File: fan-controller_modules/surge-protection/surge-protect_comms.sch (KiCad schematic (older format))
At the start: 17 parts

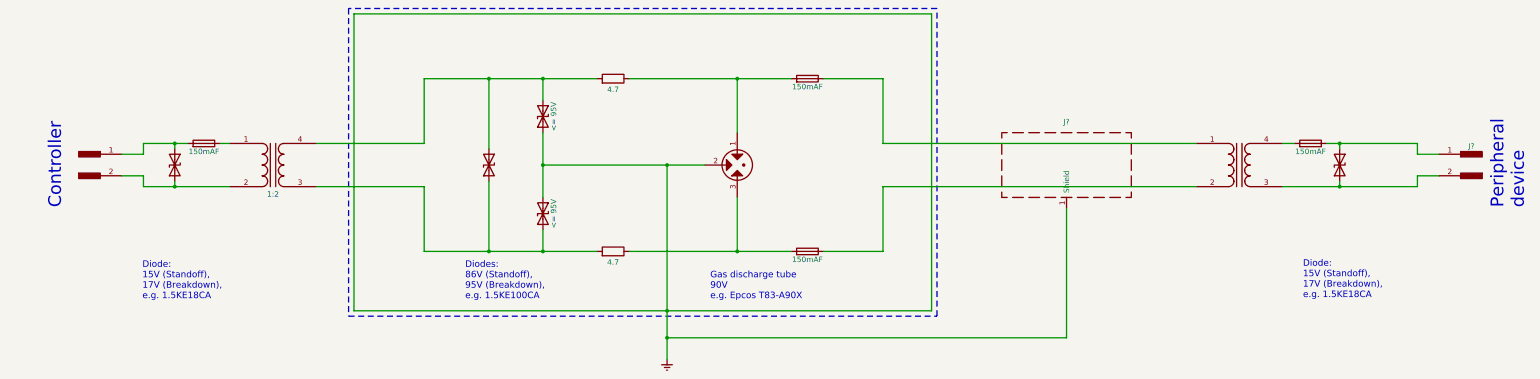
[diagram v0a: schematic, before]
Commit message: Modifying surge protection.
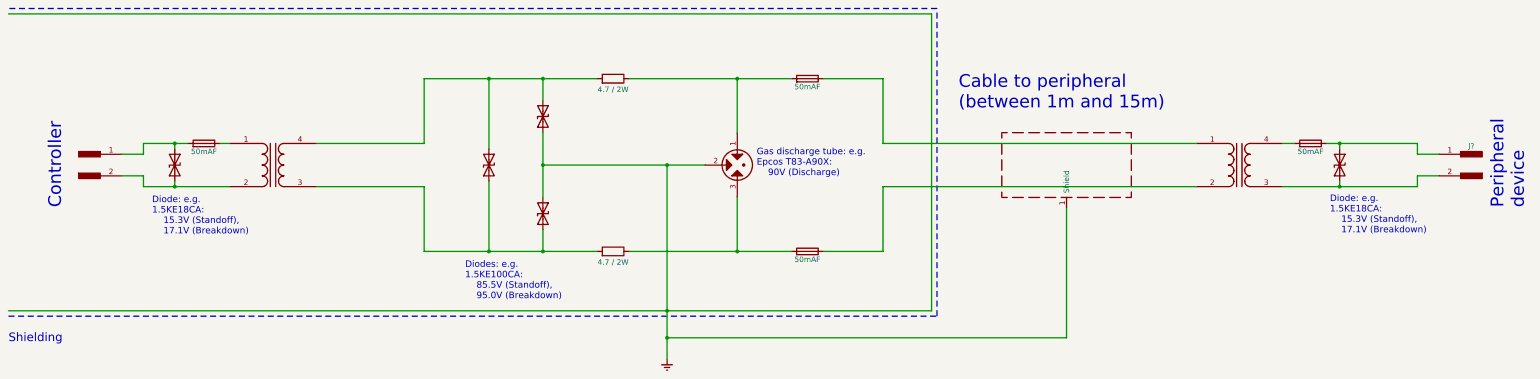
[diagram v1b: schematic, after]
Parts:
- F? (x4): value 150mAF -> 50mAF
- R? (x2): value 4.7 -> 4.7 / 2W
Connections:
- wire segments 47 -> 61
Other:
- note added: "Cable to peripheral\n(between 1m and 15m)"
- note added: "Diode: e.g. \n1.5KE18CA:\n 15.3V (Standoff),\n 17.1V (Breakdown)"
- note added: "Diode: e.g.\n1.5KE18CA:\n 15.3V (Standoff),\n 17.1V (Breakdown)"
- note added: "Diodes: e.g. \n1.5KE100CA:\n 85.5V (Standoff),\n 95.0V (Breakdown)"
- note added: "Gas discharge tube: e.g.\nEpcos T83-A90X:\n 90V (Discharge)"
- note added: "Shielding"
- note removed: "Diode: \n15V (Standoff),\n17V (Breakdown),\ne.g. 1.5KE18CA"
- note removed: "Diodes: \n86V (Standoff),\n95V (Breakdown),\ne.g. 1.5KE100CA"
- note removed: "Gas discharge tube\n90V\ne.g. Epcos T83-A90X"
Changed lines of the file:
@@
 P 6000 5100
 F 0 "D?" H 6000 5200 50  0001 C CNN
-F 1 "<= 95V" H 6000 5000 50  0000 C CNN
+F 1 "<= 95V" H 6000 5000 50  0001 C CNN
 F 2 "" H 6000 5100 50  0001 C CNN
 F 3 "" H 6000 5100 50  0001 C CNN
@@
 P 6000 6000
 F 0 "D?" H 6000 6100 50  0001 C CNN
-F 1 "<= 95V" H 6000 5900 50  0000 C CNN
+F 1 "<= 95V" H 6000 5900 50  0001 C CNN
 F 2 "" H 6000 6000 50  0001 C CNN
 F 3 "" H 6000 6000 50  0001 C CNN
@@
 P 6650 4750
 F 0 "R?" V 6730 4750 50  0001 C CNN
-F 1 "4.7" V 6550 4750 50  0000 C CNN
+F 1 "4.7 / 2W" V 6550 4750 50  0000 C CNN
 F 2 "" V 6580 4750 50  0001 C CNN
 F 3 "" H 6650 4750 50  0001 C CNN
@@
 P 6650 6350
 F 0 "R?" V 6730 6350 50  0001 C CNN
-F 1 "4.7" V 6550 6350 50  0000 C CNN
+F 1 "4.7 / 2W" V 6550 6350 50  0000 C CNN
 F 2 "" V 6580 6350 50  0001 C CNN
 F 3 "" H 6650 6350 50  0001 C CNN
@@
 P 8450 4750
 F 0 "F?" V 8530 4750 50  0001 C CNN
-F 1 "150mAF" V 8375 4750 50  0000 C CNN
+F 1 "50mAF" V 8375 4750 50  0000 C CNN
 F 2 "" V 8380 4750 50  0001 C CNN
 F 3 "" H 8450 4750 50  0001 C CNN
@@
 P 8450 6350
 F 0 "F?" V 8530 6350 50  0001 C CNN
-F 1 "150mAF" V 8375 6350 50  0000 C CNN
+F 1 "50mAF" V 8375 6350 50  0000 C CNN
 F 2 "" V 8380 6350 50  0001 C CNN
 F 3 "" H 8450 6350 50  0001 C CNN
@@
 $EndComp
 Wire Notes Line
-	4200 4100 4200 6950
-Wire Notes Line
 	9650 6950 9650 4100
-Wire Wire Line
-	4250 4150 9600 4150
-Wire Wire Line
-	9600 4150 9600 6900
-Wire Wire Line
-	9600 6900 4250 6900
-Wire Wire Line
-	4250 6900 4250 4150
 $Comp
 L Earth #PWR?
@@
 $EndComp
 Wire Wire Line
-	6800 4750 8300 4750
-Wire Wire Line
-	6800 6350 8300 6350
+	6800 4750 7800 4750
+Wire Wire Line
+	7800 4750 8300 4750
+Wire Wire Line
+	6800 6350 7800 6350
+Wire Wire Line
+	7800 6350 8300 6350
 Wire Wire Line
 	7800 5250 7800 4750
@@
 Connection ~ 7800 6350
 Wire Wire Line
-	6000 5250 6000 5850
-Wire Wire Line
-	6000 5550 7500 5550
+	6000 5250 6000 5550
+Wire Wire Line
+	6000 5550 6000 5850
+Wire Wire Line
+	6000 5550 7150 5550
+Wire Wire Line
+	7150 5550 7500 5550
 Connection ~ 6000 5550
 Wire Wire Line
 	6000 4750 6000 4950
 Wire Wire Line
-	4900 4750 6500 4750
+	4900 4750 5500 4750
+Wire Wire Line
+	5500 4750 6000 4750
+Wire Wire Line
+	6000 4750 6500 4750
 Wire Wire Line
 	6000 6350 6000 6150
 Wire Wire Line
-	4900 6350 6500 6350
+	4900 6350 5500 6350
+Wire Wire Line
+	5500 6350 6000 6350
+Wire Wire Line
+	6000 6350 6500 6350
 Wire Wire Line
 	5500 5400 5500 4750
@@
 Connection ~ 6000 6350
 Wire Wire Line
-	7150 5550 7150 7350
-Connection ~ 7150 6900
+	7150 5550 7150 6900
+Wire Wire Line
+	7150 6900 7150 7150
+Wire Wire Line
+	7150 7150 7150 7350
 Connection ~ 7150 5550
 Wire Wire Line
@@
 P 3500 5550
 F 0 "T?" H 3500 5800 50  0001 C CNN
-F 1 "1:2" H 3500 5280 50  0000 C CNN
+F 1 "1:2" H 3500 5280 50  0001 C CNN
 F 2 "" H 3500 5550 50  0001 C CNN
 F 3 "" H 3500 5550 50  0001 C CNN
@@
 	2300 5450 2300 5350
 Wire Wire Line
-	2300 5350 2710 5350
+	2300 5350 2590 5350
+Wire Wire Line
+	2590 5350 2710 5350
 Wire Wire Line
 	2100 5650 2300 5650
@@
 	2300 5650 2300 5750
 Wire Wire Line
-	2300 5750 3100 5750
-Wire Wire Line
-	12850 5750 14100 5750
+	2300 5750 2590 5750
+Wire Wire Line
+	2590 5750 3100 5750
+Wire Wire Line
+	12850 5750 13380 5750
+Wire Wire Line
+	13380 5750 14100 5750
 Wire Wire Line
 	14100 5750 14100 5650
@@
 U 1 1 5995C56A
 P 10850 5550
-F 0 "J?" H 10850 5950 50  0000 C CNN
+F 0 "J?" H 10850 5950 50  0001 C CNN
 F 1 "RF_Shield_One_Piece" H 10850 5650 50  0001 C CNN
 F 2 "" H 10850 5450 50  0001 C CNN
@@
 Connection ~ 2590 5750
 Wire Notes Line
-	9650 4100 4200 4100
+	9650 4100 1050 4100
 Wire Notes Line
-	4200 6950 9650 6950
+	1050 6950 9650 6950
 Text Notes 5280 6800 0    60   ~ 0
-Diodes: \n86V (Standoff),\n95V (Breakdown),\ne.g. 1.5KE100CA
-Text Notes 7550 6800 0    60   ~ 0
-Gas discharge tube\n90V\ne.g. Epcos T83-A90X
-Text Notes 2290 6800 0    60   ~ 0
-Diode: \n15V (Standoff),\n17V (Breakdown),\ne.g. 1.5KE18CA
+Diodes: e.g. \n1.5KE100CA:\n    85.5V (Standoff),\n    95.0V (Breakdown)
+Text Notes 2380 6200 0    60   ~ 0
+Diode: e.g.\n1.5KE18CA:\n    15.3V (Standoff),\n    17.1V (Breakdown)
 $Comp
 L Fuse F?
@@
 P 2860 5350
 F 0 "F?" V 2940 5350 50  0001 C CNN
-F 1 "150mAF" V 2785 5350 50  0000 C CNN
+F 1 "50mAF" V 2785 5350 50  0000 C CNN
 F 2 "" V 2790 5350 50  0001 C CNN
 F 3 "" H 2860 5350 50  0001 C CNN
@@
 P 13110 5350
 F 0 "F?" V 13190 5350 50  0001 C CNN
-F 1 "150mAF" V 13035 5350 50  0000 C CNN
+F 1 "50mAF" V 13035 5350 50  0000 C CNN
 F 2 "" V 13040 5350 50  0001 C CNN
 F 3 "" H 13110 5350 50  0001 C CNN
@@
 	12850 5350 12960 5350
 Wire Wire Line
-	13260 5350 14100 5350
+	13260 5350 13380 5350
+Wire Wire Line
+	13380 5350 14100 5350
 Wire Wire Line
 	13380 5350 13380 5400
@@
 	14100 5450 14100 5350
 Connection ~ 13380 5350
-Text Notes 13040 6790 0    60   ~ 0
-Diode: \n15V (Standoff),\n17V (Breakdown),\ne.g. 1.5KE18CA
+Text Notes 13290 6190 0    60   ~ 0
+Diode: e.g. \n1.5KE18CA:\n    15.3V (Standoff),\n    17.1V (Breakdown)
+Text Notes 9850 5040 0    118  ~ 0
+Cable to peripheral\n(between 1m and 15m)
+Text Notes 7980 5660 0    60   ~ 0
+Gas discharge tube: e.g.\nEpcos T83-A90X:\n    90V (Discharge)
+Connection ~ 7150 6900
+Wire Wire Line
+	7150 6900 1050 6900
+Wire Wire Line
+	9600 6900 7150 6900
+Wire Wire Line
+	9600 4150 9600 6900
+Wire Wire Line
+	1050 4150 9600 4150
+Text Notes 1050 7200 0    79   ~ 0
+Shielding
 $EndSCHEMATC
